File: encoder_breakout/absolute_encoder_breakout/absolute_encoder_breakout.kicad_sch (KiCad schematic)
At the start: 2 parts

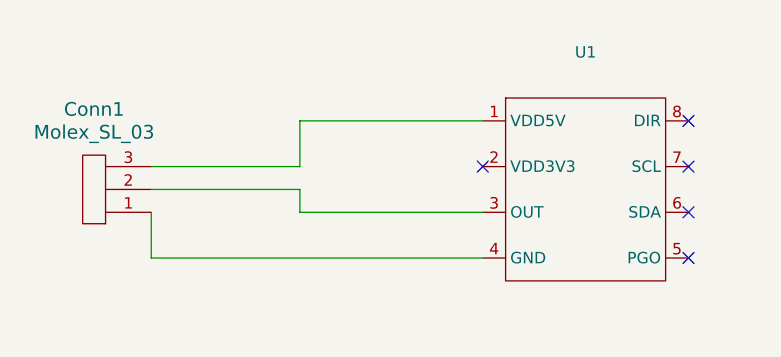
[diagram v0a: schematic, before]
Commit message: Fix Schematic after Review
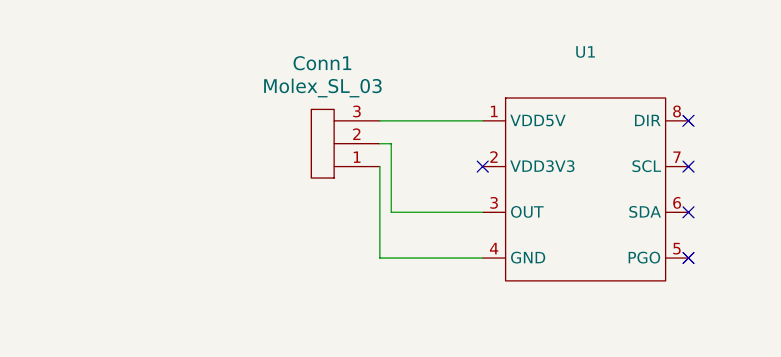
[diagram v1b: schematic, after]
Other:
- moved on the sheet: Conn1
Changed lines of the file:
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@@
 	(wire
 		(pts
-			(xy 107.95 88.9) (xy 107.95 86.36)
+			(xy 116.84 93.98) (xy 116.84 83.82)
 		)
 		(stroke
@@
 	(wire
 		(pts
-			(xy 107.95 78.74) (xy 107.95 83.82)
+			(xy 116.84 78.74) (xy 128.27 78.74)
 		)
 		(stroke
@@
 	(wire
 		(pts
-			(xy 91.44 93.98) (xy 91.44 88.9)
+			(xy 116.84 81.28) (xy 118.11 81.28)
 		)
 		(stroke
@@
 	(wire
 		(pts
-			(xy 128.27 93.98) (xy 91.44 93.98)
+			(xy 128.27 93.98) (xy 116.84 93.98)
 		)
 		(stroke
@@
 	(wire
 		(pts
-			(xy 107.95 86.36) (xy 91.44 86.36)
+			(xy 128.27 88.9) (xy 118.11 88.9)
 		)
 		(stroke
@@
 	(wire
 		(pts
-			(xy 107.95 83.82) (xy 91.44 83.82)
-		)
-		(stroke
-			(width 0)
-			(type default)
-		)
-	)
-	(wire
-		(pts
-			(xy 128.27 78.74) (xy 107.95 78.74)
-		)
-		(stroke
-			(width 0)
-			(type default)
-		)
-	)
-	(wire
-		(pts
-			(xy 128.27 88.9) (xy 107.95 88.9)
+			(xy 118.11 88.9) (xy 118.11 81.28)
 		)
 		(stroke
@@
 	(symbol
 		(lib_id "MRDT_Connectors:Molex_SL_03")
-		(at 86.36 82.55 180)
+		(at 111.76 77.47 180)
 		(unit 1)
 		(exclude_from_sim no)
@@
 		(fields_autoplaced yes)
 		(property "Reference" "Conn1"
-			(at 85.09 77.47 0)
+			(at 110.49 72.39 0)
 			(effects
 				(font
@@
 		)
 		(property "Value" "Molex_SL_03"
-			(at 85.09 80.01 0)
+			(at 110.49 74.93 0)
 			(effects
 				(font
@@
 		)
 		(property "Footprint" ""
-			(at 86.36 82.55 0)
+			(at 111.76 77.47 0)
 			(effects
 				(font
@@
 		)
 		(property "Datasheet" ""
-			(at 86.36 82.55 0)
+			(at 111.76 77.47 0)
 			(effects
 				(font
@@
 		)
 		(property "Description" ""
-			(at 86.36 82.55 0)
+			(at 111.76 77.47 0)
 			(effects
 				(font
@@
 			)
 		)
-		(property "Datasheet" ""
+		(property "Datasheet" "https://look.ams-osram.com/m/7059eac7531a86fd/original/AS5600-DS000365.pdf"
 			(at 139.7 73.66 0)
 			(effects

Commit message: Add Encoder PCB
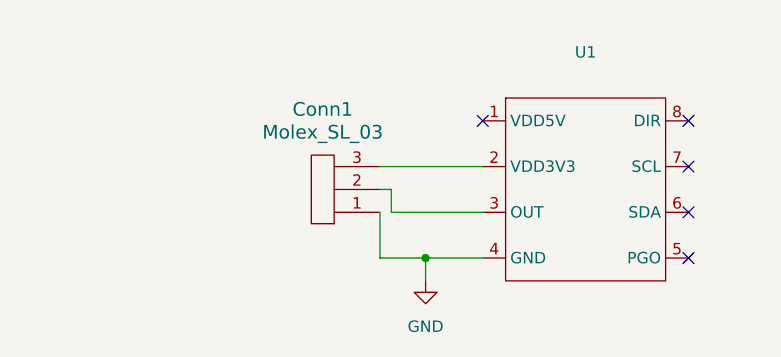
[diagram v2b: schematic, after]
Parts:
- Conn1: footprint (none) -> Connector_JST:JST_PH_B3B-PH-K_1x03_P2.00mm_Vertical
- U1: footprint (none) -> Package_SO:SOIC-8_3.9x4.9mm_P1.27mm
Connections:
- net GND: now reaches Conn1.1, U1.4 (GND)
- net at Conn1.3: now also U1.2 (VDD3V3); no longer U1.1 (VDD5V)
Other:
- moved on the sheet: Conn1
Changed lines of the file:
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@@
 	(generator_version "9.0")
 	(paper "A4")
+	(junction
+		(at 121.92 93.98)
+		(diameter 0)
+		(color 0 0 0 0)
+	)
 	(no_connect
 		(at 151.13 93.98)
@@
 	)
 	(no_connect
+		(at 128.27 78.74)
+	)
+	(no_connect
 		(at 151.13 78.74)
 	)
@@
 		(at 151.13 83.82)
 	)
-	(no_connect
-		(at 128.27 83.82)
-	)
-	(wire
-		(pts
-			(xy 116.84 93.98) (xy 116.84 83.82)
-		)
-		(stroke
-			(width 0)
-			(type default)
-		)
-	)
-	(wire
-		(pts
-			(xy 116.84 78.74) (xy 128.27 78.74)
-		)
-		(stroke
-			(width 0)
-			(type default)
-		)
-	)
-	(wire
-		(pts
-			(xy 116.84 81.28) (xy 118.11 81.28)
-		)
-		(stroke
-			(width 0)
-			(type default)
-		)
-	)
-	(wire
-		(pts
-			(xy 128.27 93.98) (xy 116.84 93.98)
+	(wire
+		(pts
+			(xy 116.84 93.98) (xy 116.84 88.9)
+		)
+		(stroke
+			(width 0)
+			(type default)
+		)
+	)
+	(wire
+		(pts
+			(xy 116.84 83.82) (xy 128.27 83.82)
+		)
+		(stroke
+			(width 0)
+			(type default)
+		)
+	)
+	(wire
+		(pts
+			(xy 116.84 86.36) (xy 118.11 86.36)
+		)
+		(stroke
+			(width 0)
+			(type default)
+		)
+	)
+	(wire
+		(pts
+			(xy 121.92 93.98) (xy 116.84 93.98)
+		)
+		(stroke
+			(width 0)
+			(type default)
+		)
+	)
+	(wire
+		(pts
+			(xy 128.27 93.98) (xy 121.92 93.98)
 		)
 		(stroke
@@
 	(wire
 		(pts
-			(xy 118.11 88.9) (xy 118.11 81.28)
+			(xy 121.92 93.98) (xy 121.92 96.52)
+		)
+		(stroke
+			(width 0)
+			(type default)
+		)
+	)
+	(wire
+		(pts
+			(xy 118.11 88.9) (xy 118.11 86.36)
 		)
 		(stroke
@@
 	(symbol
 		(lib_id "MRDT_Connectors:Molex_SL_03")
-		(at 111.76 77.47 180)
+		(at 111.76 82.55 180)
 		(unit 1)
 		(exclude_from_sim no)
@@
 		(fields_autoplaced yes)
 		(property "Reference" "Conn1"
-			(at 110.49 72.39 0)
+			(at 110.49 77.47 0)
 			(effects
 				(font
@@
 		)
 		(property "Value" "Molex_SL_03"
-			(at 110.49 74.93 0)
-			(effects
-				(font
-					(size 1.524 1.524)
-				)
-			)
-		)
-		(property "Footprint" ""
-			(at 111.76 77.47 0)
+			(at 110.49 80.01 0)
+			(effects
+				(font
+					(size 1.524 1.524)
+				)
+			)
+		)
+		(property "Footprint" "Connector_JST:JST_PH_B3B-PH-K_1x03_P2.00mm_Vertical"
+			(at 111.76 82.55 0)
 			(effects
 				(font
@@
 		)
 		(property "Datasheet" ""
-			(at 111.76 77.47 0)
+			(at 111.76 82.55 0)
 			(effects
 				(font
@@
 		)
 		(property "Description" ""
-			(at 111.76 77.47 0)
+			(at 111.76 82.55 0)
 			(effects
 				(font
@@
 			)
 		)
-		(property "Footprint" ""
+		(property "Footprint" "Package_SO:SOIC-8_3.9x4.9mm_P1.27mm"
 			(at 139.7 73.66 0)
 			(effects
@@
 					(unit 1)
 				)
+			)
+		)
+	)
+	(symbol
+		(lib_id "power:GND")
+		(at 121.92 96.52 0)
+		(unit 1)
+		(exclude_from_sim no)
+		(in_bom yes)
+		(on_board yes)
+		(dnp no)
+		(fields_autoplaced yes)
+		(property "Reference" "#PWR01"
+			(at 121.92 102.87 0)
+			(effects
+				(font
+					(size 1.27 1.27)
+				)
+				(hide yes)
+			)
+		)
+		(property "Value" "GND"
+			(at 121.92 101.6 0)
+			(effects
+				(font
+					(size 1.27 1.27)
+				)
+			)
+		)
+		(property "Footprint" ""
+			(at 121.92 96.52 0)
+			(effects
+				(font
+					(size 1.27 1.27)
+				)
+				(hide yes)
+			)
+		)
+		(property "Datasheet" ""
+			(at 121.92 96.52 0)
+			(effects
+				(font
+					(size 1.27 1.27)
+				)
+				(hide yes)
+			)
+		)
+		(property "Description" "Power symbol creates a global label with name \"GND\" , ground"
+			(at 121.92 96.52 0)
+			(effects
+				(font
+					(size 1.27 1.27)
+				)
+				(hide yes)
+			)
+		)
+		(pin "1"
+		)
+		(instances
+			(project ""
+				(path "/ebb075bd-427b-4233-b984-4ab8b040b824"
+					(reference "#PWR01")
+					(unit 1)
+				)

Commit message: Fix Breakout Schematic and Layout
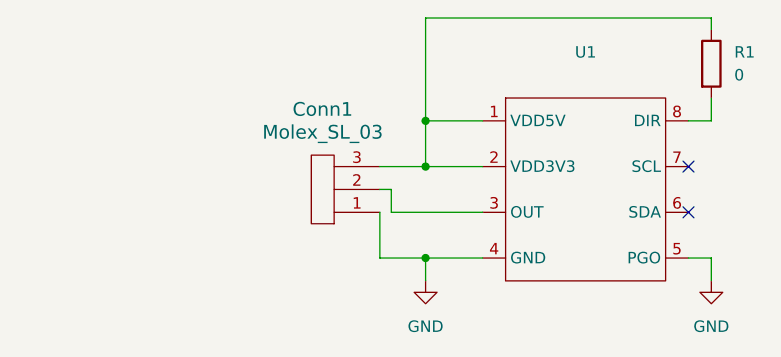
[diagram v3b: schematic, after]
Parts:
- added R1: 0, symbol Device:R
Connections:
- net GND: now also U1.5 (PGO)
- net at Conn1.3, U1.2 (VDD3V3): now also U1.1 (VDD5V), R1.1
- net at U1.8 (DIR): now also R1.2
- no-connect marks 5 -> 2
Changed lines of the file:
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@@
 	(paper "A4")
+	(junction
+		(at 121.92 78.74)
+		(diameter 0)
+		(color 0 0 0 0)
+	)
+	(junction
+		(at 121.92 83.82)
+		(diameter 0)
+		(color 0 0 0 0)
+	)
 	(junction
 		(at 121.92 93.98)
@@
 	)
 	(no_connect
-		(at 151.13 93.98)
-	)
-	(no_connect
 		(at 151.13 88.9)
-	)
-	(no_connect
-		(at 128.27 78.74)
-	)
-	(no_connect
-		(at 151.13 78.74)
 	)
 	(no_connect
@@
 	(wire
 		(pts
+			(xy 121.92 78.74) (xy 121.92 67.31)
+		)
+		(stroke
+			(width 0)
+			(type default)
+		)
+	)
+	(wire
+		(pts
+			(xy 121.92 67.31) (xy 153.67 67.31)
+		)
+		(stroke
+			(width 0)
+			(type default)
+		)
+	)
+	(wire
+		(pts
+			(xy 128.27 78.74) (xy 121.92 78.74)
+		)
+		(stroke
+			(width 0)
+			(type default)
+		)
+	)
+	(wire
+		(pts
+			(xy 151.13 78.74) (xy 153.67 78.74)
+		)
+		(stroke
+			(width 0)
+			(type default)
+		)
+	)
+	(wire
+		(pts
 			(xy 116.84 93.98) (xy 116.84 88.9)
 		)
@@
 	(wire
 		(pts
-			(xy 116.84 83.82) (xy 128.27 83.82)
+			(xy 153.67 76.2) (xy 153.67 78.74)
+		)
+		(stroke
+			(width 0)
+			(type default)
+		)
+	)
+	(wire
+		(pts
+			(xy 116.84 83.82) (xy 121.92 83.82)
+		)
+		(stroke
+			(width 0)
+			(type default)
+		)
+	)
+	(wire
+		(pts
+			(xy 153.67 67.31) (xy 153.67 68.58)
+		)
+		(stroke
+			(width 0)
+			(type default)
+		)
+	)
+	(wire
+		(pts
+			(xy 151.13 93.98) (xy 153.67 93.98)
 		)
 		(stroke
@@
 	(wire
 		(pts
+			(xy 121.92 78.74) (xy 121.92 83.82)
+		)
+		(stroke
+			(width 0)
+			(type default)
+		)
+	)
+	(wire
+		(pts
 			(xy 121.92 93.98) (xy 116.84 93.98)
 		)
@@
 	(wire
 		(pts
+			(xy 153.67 93.98) (xy 153.67 96.52)
+		)
+		(stroke
+			(width 0)
+			(type default)
+		)
+	)
+	(wire
+		(pts
 			(xy 121.92 93.98) (xy 121.92 96.52)
 		)
@@
 	(wire
 		(pts
+			(xy 121.92 83.82) (xy 128.27 83.82)
+		)
+		(stroke
+			(width 0)
+			(type default)
+		)
+	)
+	(wire
+		(pts
 			(xy 118.11 88.9) (xy 118.11 86.36)
 		)
@@
 			(width 0)
 			(type default)
+		)
+	)
+	(symbol
+		(lib_id "power:GND")
+		(at 153.67 96.52 0)
+		(unit 1)
+		(exclude_from_sim no)
+		(in_bom yes)
+		(on_board yes)
+		(dnp no)
+		(fields_autoplaced yes)
+		(property "Reference" "#PWR02"
+			(at 153.67 102.87 0)
+			(effects
+				(font
+					(size 1.27 1.27)
+				)
+				(hide yes)
+			)
+		)
+		(property "Value" "GND"
+			(at 153.67 101.6 0)
+			(effects
+				(font
+					(size 1.27 1.27)
+				)
+			)
+		)
+		(property "Footprint" ""
+			(at 153.67 96.52 0)
+			(effects
+				(font
+					(size 1.27 1.27)
+				)
+				(hide yes)
+			)
+		)
+		(property "Datasheet" ""
+			(at 153.67 96.52 0)
+			(effects
+				(font
+					(size 1.27 1.27)
+				)
+				(hide yes)
+			)
+		)
+		(property "Description" "Power symbol creates a global label with name \"GND\" , ground"
+			(at 153.67 96.52 0)
+			(effects
+				(font
+					(size 1.27 1.27)
+				)
+				(hide yes)
+			)
+		)
+		(pin "1"
+		)
+		(instances
+			(project "absolute_encoder_breakout"
+				(path "/ebb075bd-427b-4233-b984-4ab8b040b824"
+					(reference "#PWR02")
+					(unit 1)
+				)
+			)
 		)
 	)
@@
 					(unit 1)
 				)
+			)
+		)
+	)
+	(symbol
+		(lib_id "Device:R")
+		(at 153.67 72.39 0)
+		(unit 1)
+		(exclude_from_sim no)
+		(in_bom yes)
+		(on_board yes)
+		(dnp no)
+		(fields_autoplaced yes)
+		(property "Reference" "R1"
+			(at 156.21 71.1199 0)
+			(effects
+				(font
+					(size 1.27 1.27)
+				)
+				(justify left)
+			)
+		)
+		(property "Value" "0"
+			(at 156.21 73.6599 0)
+			(effects
+				(font
+					(size 1.27 1.27)
+				)
+				(justify left)
+			)
+		)
+		(property "Footprint" ""
+			(at 151.892 72.39 90)
+			(effects
+				(font
+					(size 1.27 1.27)
+				)
+				(hide yes)
+			)
+		)
+		(property "Datasheet" "~"
+			(at 153.67 72.39 0)
+			(effects
+				(font
+					(size 1.27 1.27)
+				)
+				(hide yes)
+			)
+		)
+		(property "Description" "Resistor"
+			(at 153.67 72.39 0)
+			(effects
+				(font
+					(size 1.27 1.27)
+				)
+				(hide yes)
+			)
+		)
+		(pin "2"
+		)
+		(pin "1"
+		)
+		(instances
+			(project ""
+				(path "/ebb075bd-427b-4233-b984-4ab8b040b824"
+					(reference "R1")
+					(unit 1)
+				)

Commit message: Fix Breakout
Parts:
- R1: footprint (none) -> Resistor_SMD:R_0603_1608Metric_Pad0.98x0.95mm_HandSolder
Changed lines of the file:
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@@
 			)
 		)
-		(property "Footprint" ""
+		(property "Footprint" "Resistor_SMD:R_0603_1608Metric_Pad0.98x0.95mm_HandSolder"
 			(at 151.892 72.39 90)
 			(effects

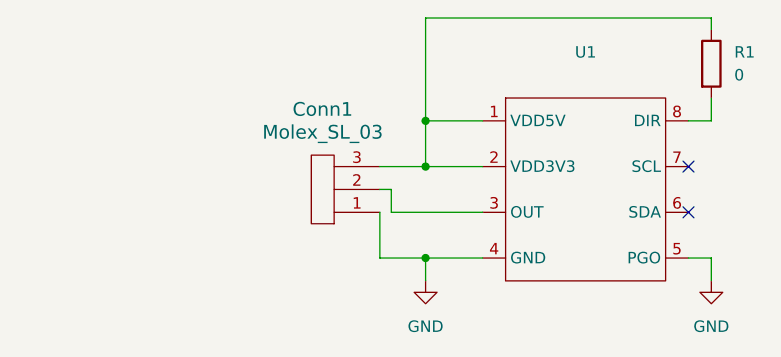
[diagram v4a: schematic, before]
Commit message: add I2C bus, reverted encoder breakout
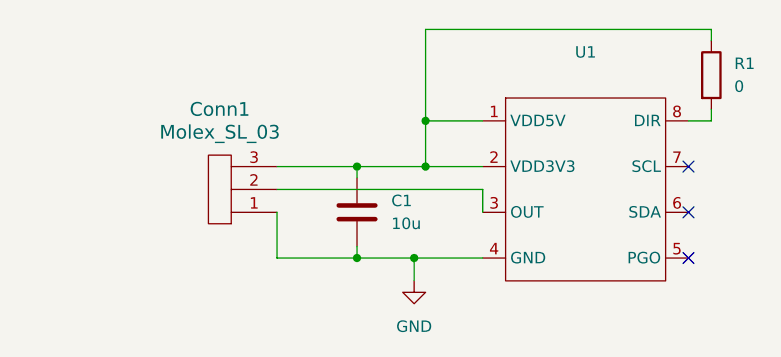
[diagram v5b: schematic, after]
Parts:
- added C1: 10u, symbol Device:C
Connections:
- net GND: now also C1.2; no longer U1.5 (PGO)
- net at Conn1.3, R1.1, U1.1 (VDD5V)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: now also C1.1
- no-connect marks 2 -> 3
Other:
- moved on the sheet: Conn1, R1
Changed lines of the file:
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@@
 	)
 	(junction
-		(at 121.92 93.98)
+		(at 114.3 93.98)
 		(diameter 0)
 		(color 0 0 0 0)
 	)
+	(junction
+		(at 114.3 83.82)
+		(diameter 0)
+		(color 0 0 0 0)
+	)
+	(junction
+		(at 120.65 93.98)
+		(diameter 0)
+		(color 0 0 0 0)
+	)
+	(no_connect
+		(at 151.13 93.98)
+	)
 	(no_connect
 		(at 151.13 88.9)
@@
 	(wire
 		(pts
-			(xy 121.92 78.74) (xy 121.92 67.31)
-		)
-		(stroke
-			(width 0)
-			(type default)
-		)
-	)
-	(wire
-		(pts
-			(xy 121.92 67.31) (xy 153.67 67.31)
+			(xy 121.92 78.74) (xy 121.92 68.58)
+		)
+		(stroke
+			(width 0)
+			(type default)
+		)
+	)
+	(wire
+		(pts
+			(xy 121.92 68.58) (xy 153.67 68.58)
 		)
 		(stroke
@@
 	(wire
 		(pts
-			(xy 116.84 93.98) (xy 116.84 88.9)
-		)
-		(stroke
-			(width 0)
-			(type default)
-		)
-	)
-	(wire
-		(pts
-			(xy 153.67 76.2) (xy 153.67 78.74)
-		)
-		(stroke
-			(width 0)
-			(type default)
-		)
-	)
-	(wire
-		(pts
-			(xy 116.84 83.82) (xy 121.92 83.82)
-		)
-		(stroke
-			(width 0)
-			(type default)
-		)
-	)
-	(wire
-		(pts
-			(xy 153.67 67.31) (xy 153.67 68.58)
-		)
-		(stroke
-			(width 0)
-			(type default)
-		)
-	)
-	(wire
-		(pts
-			(xy 151.13 93.98) (xy 153.67 93.98)
-		)
-		(stroke
-			(width 0)
-			(type default)
-		)
-	)
-	(wire
-		(pts
-			(xy 116.84 86.36) (xy 118.11 86.36)
+			(xy 120.65 93.98) (xy 128.27 93.98)
+		)
+		(stroke
+			(width 0)
+			(type default)
+		)
+	)
+	(wire
+		(pts
+			(xy 105.41 93.98) (xy 114.3 93.98)
+		)
+		(stroke
+			(width 0)
+			(type default)
+		)
+	)
+	(wire
+		(pts
+			(xy 105.41 93.98) (xy 105.41 88.9)
+		)
+		(stroke
+			(width 0)
+			(type default)
+		)
+	)
+	(wire
+		(pts
+			(xy 105.41 86.36) (xy 128.27 86.36)
+		)
+		(stroke
+			(width 0)
+			(type default)
+		)
+	)
+	(wire
+		(pts
+			(xy 105.41 83.82) (xy 114.3 83.82)
+		)
+		(stroke
+			(width 0)
+			(type default)
+		)
+	)
+	(wire
+		(pts
+			(xy 114.3 83.82) (xy 121.92 83.82)
+		)
+		(stroke
+			(width 0)
+			(type default)
+		)
+	)
+	(wire
+		(pts
+			(xy 153.67 68.58) (xy 153.67 69.85)
 		)
 		(stroke
@@
 	(wire
 		(pts
-			(xy 121.92 93.98) (xy 116.84 93.98)
-		)
-		(stroke
-			(width 0)
-			(type default)
-		)
-	)
-	(wire
-		(pts
-			(xy 128.27 93.98) (xy 121.92 93.98)
-		)
-		(stroke
-			(width 0)
-			(type default)
-		)
-	)
-	(wire
-		(pts
-			(xy 128.27 88.9) (xy 118.11 88.9)
-		)
-		(stroke
-			(width 0)
-			(type default)
-		)
-	)
-	(wire
-		(pts
-			(xy 153.67 93.98) (xy 153.67 96.52)
-		)
-		(stroke
-			(width 0)
-			(type default)
-		)
-	)
-	(wire
-		(pts
-			(xy 121.92 93.98) (xy 121.92 96.52)
+			(xy 128.27 86.36) (xy 128.27 88.9)
+		)
+		(stroke
+			(width 0)
+			(type default)
+		)
+	)
+	(wire
+		(pts
+			(xy 153.67 77.47) (xy 153.67 78.74)
+		)
+		(stroke
+			(width 0)
+			(type default)
+		)
+	)
+	(wire
+		(pts
+			(xy 120.65 93.98) (xy 120.65 96.52)
 		)
 		(stroke
@@
 	(wire
 		(pts
-			(xy 118.11 88.9) (xy 118.11 86.36)
+			(xy 114.3 83.82) (xy 114.3 85.09)
+		)
+		(stroke
+			(width 0)
+			(type default)
+		)
+	)
+	(wire
+		(pts
+			(xy 114.3 93.98) (xy 120.65 93.98)
+		)
+		(stroke
+			(width 0)
+			(type default)
+		)
+	)
+	(wire
+		(pts
+			(xy 114.3 92.71) (xy 114.3 93.98)
 		)
 		(stroke
@@
 	)
 	(symbol
-		(lib_id "power:GND")
-		(at 153.67 96.52 0)
+		(lib_id "Device:C")
+		(at 114.3 88.9 0)
 		(unit 1)
 		(exclude_from_sim no)
@@
 		(dnp no)
 		(fields_autoplaced yes)
-		(property "Reference" "#PWR02"
-			(at 153.67 102.87 0)
-			(effects
-				(font
-					(size 1.27 1.27)
-				)
-				(hide yes)
-			)
-		)
-		(property "Value" "GND"
-			(at 153.67 101.6 0)
-			(effects
-				(font
-					(size 1.27 1.27)
-				)
+		(property "Reference" "C1"
+			(at 118.11 87.6299 0)
+			(effects
+				(font
+					(size 1.27 1.27)
+				)
+				(justify left)
+			)
+		)
+		(property "Value" "10u"
+			(at 118.11 90.1699 0)
+			(effects
+				(font
+					(size 1.27 1.27)
+				)
+				(justify left)
 			)
 		)
 		(property "Footprint" ""
-			(at 153.67 96.52 0)
-			(effects
-				(font
-					(size 1.27 1.27)
-				)
-				(hide yes)
-			)
-		)
-		(property "Datasheet" ""
-			(at 153.67 96.52 0)
-			(effects
-				(font
-					(size 1.27 1.27)
-				)
-				(hide yes)
-			)
-		)
-		(property "Description" "Power symbol creates a global label with name \"GND\" , ground"
-			(at 153.67 96.52 0)
+			(at 115.2652 92.71 0)
+			(effects
+				(font
+					(size 1.27 1.27)
+				)
+				(hide yes)
+			)
+		)
+		(property "Datasheet" "~"
+			(at 114.3 88.9 0)
+			(effects
+				(font
+					(size 1.27 1.27)
+				)
+				(hide yes)
+			)
+		)
+		(property "Description" "Unpolarized capacitor"
+			(at 114.3 88.9 0)
 			(effects
 				(font
@@
 		(pin "1"
 		)
+		(pin "2"
+		)
 		(instances
-			(project "absolute_encoder_breakout"
+			(project ""
 				(path "/ebb075bd-427b-4233-b984-4ab8b040b824"
-					(reference "#PWR02")
+					(reference "C1")
 					(unit 1)
 				)
@@
 	(symbol
 		(lib_id "MRDT_Connectors:Molex_SL_03")
-		(at 111.76 82.55 180)
+		(at 100.33 82.55 180)
 		(unit 1)
 		(exclude_from_sim no)
@@
 		(fields_autoplaced yes)
 		(property "Reference" "Conn1"
-			(at 110.49 77.47 0)
+			(at 99.06 77.47 0)
 			(effects
 				(font
@@
 		)
 		(property "Value" "Molex_SL_03"
-			(at 110.49 80.01 0)
+			(at 99.06 80.01 0)
 			(effects
 				(font
@@
 		)
 		(property "Footprint" "Connector_JST:JST_PH_B3B-PH-K_1x03_P2.00mm_Vertical"
-			(at 111.76 82.55 0)
+			(at 100.33 82.55 0)
 			(effects
 				(font
@@
 		)
 		(property "Datasheet" ""
-			(at 111.76 82.55 0)
+			(at 100.33 82.55 0)
 			(effects
 				(font
@@
 		)
 		(property "Description" ""
-			(at 111.76 82.55 0)
+			(at 100.33 82.55 0)
 			(effects
 				(font
@@
 	(symbol
 		(lib_id "power:GND")
-		(at 121.92 96.52 0)
+		(at 120.65 96.52 0)
 		(unit 1)
 		(exclude_from_sim no)
@@
 		(fields_autoplaced yes)
 		(property "Reference" "#PWR01"
-			(at 121.92 102.87 0)
+			(at 120.65 102.87 0)
 			(effects
 				(font
@@
 		)
 		(property "Value" "GND"
-			(at 121.92 101.6 0)
+			(at 120.65 101.6 0)
 			(effects
 				(font
@@
 		)
 		(property "Footprint" ""
-			(at 121.92 96.52 0)
+			(at 120.65 96.52 0)
 			(effects
 				(font
@@
 		)
 		(property "Datasheet" ""
-			(at 121.92 96.52 0)
+			(at 120.65 96.52 0)
 			(effects
 				(font
@@
 		)
 		(property "Description" "Power symbol creates a global label with name \"GND\" , ground"
-			(at 121.92 96.52 0)
+			(at 120.65 96.52 0)
 			(effects
 				(font
@@
 	(symbol
 		(lib_id "Device:R")
-		(at 153.67 72.39 0)
+		(at 153.67 73.66 0)
 		(unit 1)
 		(exclude_from_sim no)
@@
 		(fields_autoplaced yes)
 		(property "Reference" "R1"
-			(at 156.21 71.1199 0)
+			(at 156.21 72.3899 0)
 			(effects
 				(font
@@
 		)
 		(property "Value" "0"
-			(at 156.21 73.6599 0)
+			(at 156.21 74.9299 0)
 			(effects
 				(font
@@
 		)
 		(property "Footprint" "Resistor_SMD:R_0603_1608Metric_Pad0.98x0.95mm_HandSolder"
-			(at 151.892 72.39 90)
+			(at 151.892 73.66 90)
 			(effects
 				(font
@@
 		)
 		(property "Datasheet" "~"
-			(at 153.67 72.39 0)
+			(at 153.67 73.66 0)
 			(effects
 				(font
@@
 		)
 		(property "Description" "Resistor"
-			(at 153.67 72.39 0)
-			(effects
-				(font
+			(at 153.67 73.66 0)
+			(effects
+				(font

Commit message: Adjust main board size
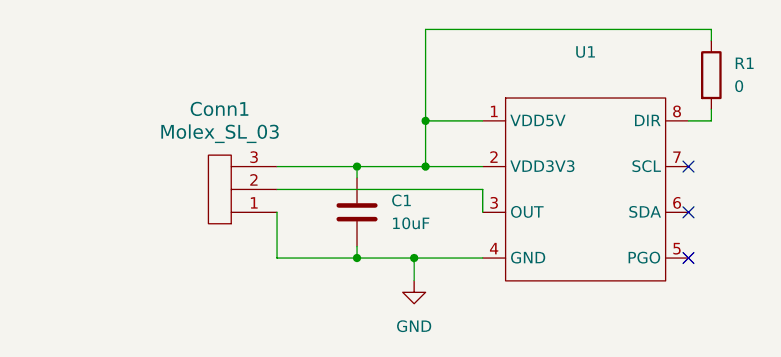
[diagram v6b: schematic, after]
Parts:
- C1: value 10u -> 10uF
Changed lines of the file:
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@@
 			)
 		)
-		(property "Value" "10u"
+		(property "Value" "10uF"
 			(at 118.11 90.1699 0)
 			(effects
